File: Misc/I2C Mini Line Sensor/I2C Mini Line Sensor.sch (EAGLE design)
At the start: 16 parts, among them U1 ADS1015.RUG, U2 QRE1113, U3 QRE1113, U4 QRE1113, U5 QRE1113

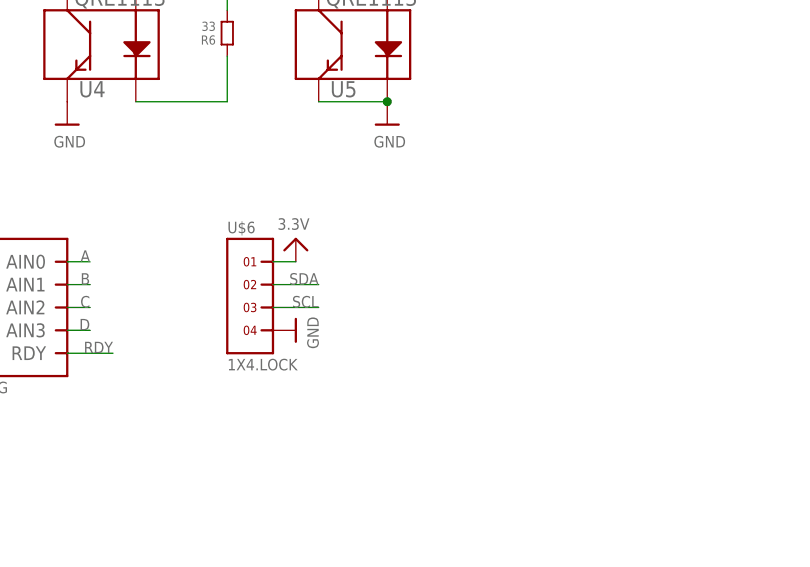
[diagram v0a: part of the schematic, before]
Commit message: Added address select pins for IC
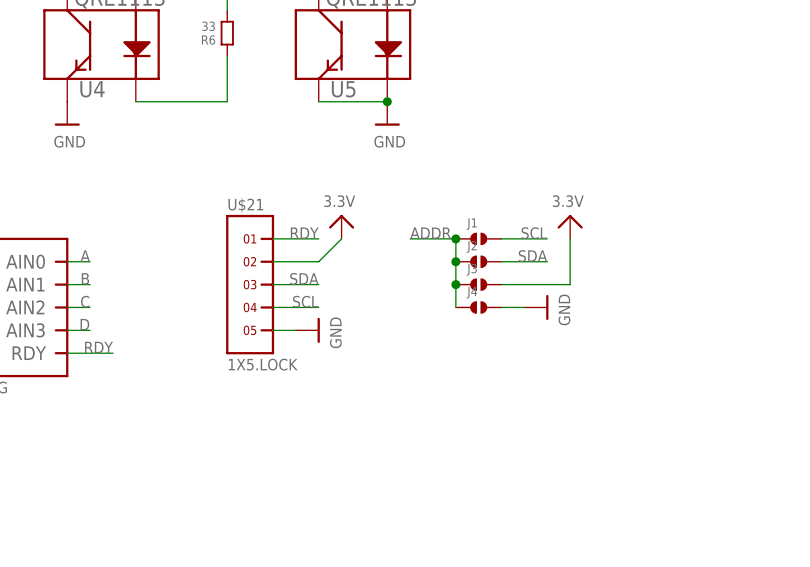
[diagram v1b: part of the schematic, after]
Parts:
- removed U$6: 1X4.LOCK, headers(.1in):1X4.LOCK
- added J1, J2, J3, J4: (no value), solderjumper:SOLDERJUMPER.2.MED
- added U$21: 1X5.LOCK, headers(.1in):1X5.LOCK
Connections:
- net 3.3V: now also J3.2, U$21.2; no longer U$6.1
- net ADDR: now also J1.1, J2.1, J3.1, J4.1
- net GND: now also J4.2, U$21.5; no longer U$6.4
- net RDY: now also U$21.1
- net SCL: now also J1.2, U$21.4; no longer U$6.3
- net SDA: now also J2.2, U$21.3; no longer U$6.2
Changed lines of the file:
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@@
 <part name="U$4" library="microbuilder" deviceset="GND" device=""/>
 <part name="U$5" library="microbuilder" deviceset="3.3V" device=""/>
-<part name="U$6" library="headers(.1in)" deviceset="1X4" device=".LOCK" value="1X4.LOCK"/>
 <part name="U$10" library="microbuilder" deviceset="GND" device=""/>
 <part name="U$11" library="microbuilder" deviceset="3.3V" device=""/>
@@
 <part name="U$15" library="microbuilder" deviceset="GND" device=""/>
 <part name="U$16" library="microbuilder" deviceset="GND" device=""/>
+<part name="J1" library="solderjumper" deviceset="SOLDERJUMPER.2" device=".MED"/>
+<part name="J2" library="solderjumper" deviceset="SOLDERJUMPER.2" device=".MED"/>
+<part name="J3" library="solderjumper" deviceset="SOLDERJUMPER.2" device=".MED"/>
+<part name="J4" library="solderjumper" deviceset="SOLDERJUMPER.2" device=".MED"/>
+<part name="U$17" library="microbuilder" deviceset="3.3V" device=""/>
+<part name="U$20" library="microbuilder" deviceset="GND" device=""/>
+<part name="U$21" library="headers(.1in)" deviceset="1X5" device=".LOCK"/>
 </parts>
 <sheets>
@@
 <instance part="U$4" gate="G$1" x="25.4" y="91.44"/>
 <instance part="U$5" gate="G$1" x="25.4" y="99.06"/>
-<instance part="U$6" gate="G$1" x="86.36" y="96.52"/>
-<instance part="U$10" gate="G$1" x="91.44" y="93.98" rot="MR270"/>
-<instance part="U$11" gate="G$1" x="91.44" y="101.6" rot="MR0"/>
+<instance part="U$10" gate="G$1" x="93.98" y="93.98" rot="MR270"/>
+<instance part="U$11" gate="G$1" x="96.52" y="104.14" rot="MR0"/>
 <instance part="U1" gate="G$1" x="55.88" y="96.52"/>
 <instance part="U$1" gate="G$1" x="45.72" y="104.14"/>
@@
 <instance part="U$15" gate="G$1" x="17.78" y="116.84"/>
 <instance part="U$16" gate="G$1" x="66.04" y="116.84"/>
+<instance part="J1" gate="G$1" x="111.76" y="104.14"/>
+<instance part="J2" gate="G$1" x="111.76" y="101.6"/>
+<instance part="J3" gate="G$1" x="111.76" y="99.06"/>
+<instance part="J4" gate="G$1" x="111.76" y="96.52"/>
+<instance part="U$17" gate="G$1" x="121.92" y="104.14" rot="MR0"/>
+<instance part="U$20" gate="G$1" x="119.38" y="96.52" rot="MR270"/>
+<instance part="U$21" gate="G$1" x="86.36" y="99.06"/>
 </instances>
 <busses>
@@
 </segment>
 <segment>
-<pinref part="U$6" gate="G$1" pin="4"/>
-<pinref part="U$10" gate="G$1" pin="GND"/>
-</segment>
-<segment>
 <pinref part="U1" gate="G$1" pin="GND"/>
 <pinref part="U$14" gate="G$1" pin="GND"/>
@@
 <pinref part="U$16" gate="G$1" pin="GND"/>
 </segment>
+<segment>
+<pinref part="U$20" gate="G$1" pin="GND"/>
+<pinref part="J4" gate="G$1" pin="2"/>
+<wire x1="116.84" y1="96.52" x2="114.3" y2="96.52" width="0.1524" layer="91"/>
+</segment>
+<segment>
+<pinref part="U$10" gate="G$1" pin="GND"/>
+<pinref part="U$21" gate="G$1" pin="5"/>
+<wire x1="91.44" y1="93.98" x2="88.9" y2="93.98" width="0.1524" layer="91"/>
+</segment>
 </net>
 <net name="SDA" class="0">
 <segment>
-<pinref part="U$6" gate="G$1" pin="2"/>
 <wire x1="88.9" y1="99.06" x2="93.98" y2="99.06" width="0.1524" layer="91"/>
 <label x="93.98" y="99.06" size="1.27" layer="95" rot="MR0"/>
+<pinref part="U$21" gate="G$1" pin="3"/>
 </segment>
 <segment>
@@
 <label x="43.18" y="99.06" size="1.27" layer="95"/>
 </segment>
+<segment>
+<pinref part="J2" gate="G$1" pin="2"/>
+<wire x1="119.38" y1="101.6" x2="114.3" y2="101.6" width="0.1524" layer="91"/>
+<label x="119.38" y="101.6" size="1.27" layer="95" rot="MR0"/>
+</segment>
 </net>
 <net name="SCL" class="0">
 <segment>
-<pinref part="U$6" gate="G$1" pin="3"/>
 <wire x1="93.98" y1="96.52" x2="88.9" y2="96.52" width="0.1524" layer="91"/>
 <label x="93.98" y="96.52" size="1.27" layer="95" rot="MR0"/>
+<pinref part="U$21" gate="G$1" pin="4"/>
 </segment>
 <segment>
@@
 <wire x1="43.18" y1="96.52" x2="48.26" y2="96.52" width="0.1524" layer="91"/>
 <label x="43.18" y="96.52" size="1.27" layer="95"/>
+</segment>
+<segment>
+<pinref part="J1" gate="G$1" pin="2"/>
+<wire x1="114.3" y1="104.14" x2="119.38" y2="104.14" width="0.1524" layer="91"/>
+<label x="119.38" y="104.14" size="1.27" layer="95" rot="MR0"/>
 </segment>
 </net>
@@
 </segment>
 <segment>
-<pinref part="U$6" gate="G$1" pin="1"/>
 <pinref part="U$11" gate="G$1" pin="3.3V"/>
-<wire x1="88.9" y1="101.6" x2="91.44" y2="101.6" width="0.1524" layer="91"/>
+<wire x1="88.9" y1="101.6" x2="93.98" y2="101.6" width="0.1524" layer="91"/>
+<wire x1="93.98" y1="101.6" x2="96.52" y2="104.14" width="0.1524" layer="91"/>
+<pinref part="U$21" gate="G$1" pin="2"/>
 </segment>
 <segment>
@@
 <pinref part="U$13" gate="G$1" pin="3.3V"/>
 </segment>
+<segment>
+<pinref part="J3" gate="G$1" pin="2"/>
+<pinref part="U$17" gate="G$1" pin="3.3V"/>
+<wire x1="114.3" y1="99.06" x2="121.92" y2="99.06" width="0.1524" layer="91"/>
+<wire x1="121.92" y1="99.06" x2="121.92" y2="104.14" width="0.1524" layer="91"/>
+</segment>
 </net>
 <net name="ADDR" class="0">
@@
 <label x="43.18" y="93.98" size="1.27" layer="95"/>
 </segment>
+<segment>
+<pinref part="J1" gate="G$1" pin="1"/>
+<pinref part="J2" gate="G$1" pin="1"/>
+<wire x1="109.22" y1="104.14" x2="109.22" y2="101.6" width="0.1524" layer="91"/>
+<pinref part="J3" gate="G$1" pin="1"/>
+<wire x1="109.22" y1="101.6" x2="109.22" y2="99.06" width="0.1524" layer="91"/>
+<junction x="109.22" y="101.6"/>
+<pinref part="J4" gate="G$1" pin="1"/>
+<wire x1="109.22" y1="99.06" x2="109.22" y2="96.52" width="0.1524" layer="91"/>
+<junction x="109.22" y="99.06"/>
+<wire x1="109.22" y1="104.14" x2="104.14" y2="104.14" width="0.1524" layer="91"/>
+<junction x="109.22" y="104.14"/>
+<label x="104.14" y="104.14" size="1.27" layer="95"/>
+</segment>
 </net>
 <net name="RDY" class="0">
@@
 <label x="71.12" y="91.44" size="1.27" layer="95" rot="MR0"/>
 </segment>
-</net>
+<segment>
+<pinref part="U$21" gate="G$1" pin="1"/>
+<wire x1="88.9" y1="104.14" x2="93.98" y2="104.14" width="0.1524" layer="91"/>
+<label x="93.98" y="104.14" size="1.27" layer="95" rot="MR0"/>
+</segment>
+</net>

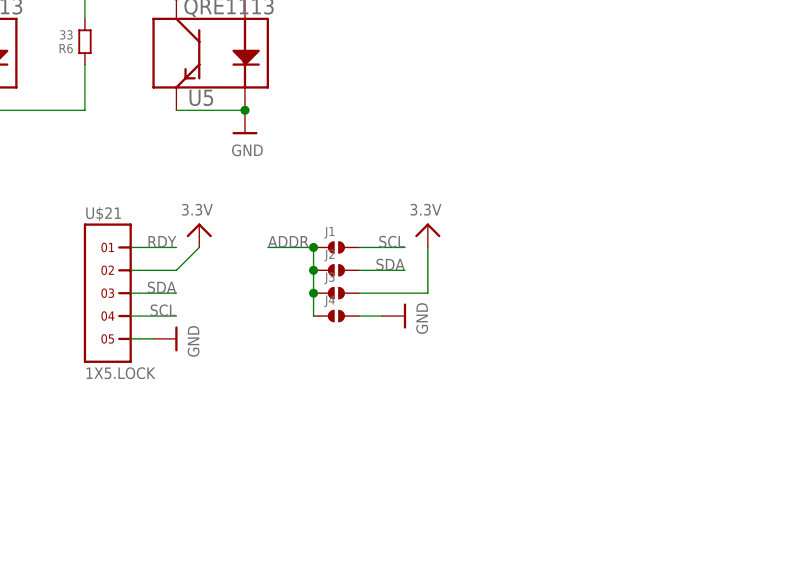
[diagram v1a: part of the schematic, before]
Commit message: Cleaned up layout of I2C Mini Line Sensor and I2C Line Sensor Also geenerated preview images
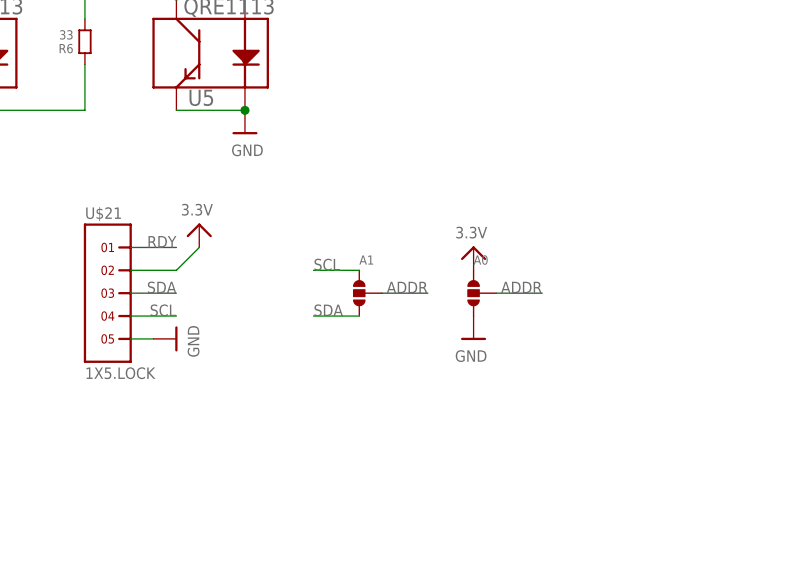
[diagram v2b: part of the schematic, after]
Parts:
- removed J1, J2, J3, J4: (no value), solderjumper:SOLDERJUMPER.2.MED
- added A0, A1: (no value), solderjumper:SOLDERJUMPER.3.MED
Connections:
- net 3.3V: now also A0.1; no longer J3.2
- net ADDR: now also A0.2, A1.2; no longer J1.1, J2.1, J3.1, J4.1
- net GND: now also A0.3; no longer J4.2
- net SCL: now also A1.1; no longer J1.2
- net SDA: now also A1.3; no longer J2.2
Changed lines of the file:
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@@
 <part name="U$15" library="microbuilder" deviceset="GND" device=""/>
 <part name="U$16" library="microbuilder" deviceset="GND" device=""/>
-<part name="J1" library="solderjumper" deviceset="SOLDERJUMPER.2" device=".MED"/>
-<part name="J2" library="solderjumper" deviceset="SOLDERJUMPER.2" device=".MED"/>
-<part name="J3" library="solderjumper" deviceset="SOLDERJUMPER.2" device=".MED"/>
-<part name="J4" library="solderjumper" deviceset="SOLDERJUMPER.2" device=".MED"/>
 <part name="U$17" library="microbuilder" deviceset="3.3V" device=""/>
 <part name="U$20" library="microbuilder" deviceset="GND" device=""/>
 <part name="U$21" library="headers(.1in)" deviceset="1X5" device=".LOCK"/>
+<part name="A1" library="solderjumper" deviceset="SOLDERJUMPER.3" device=".MED"/>
+<part name="A0" library="solderjumper" deviceset="SOLDERJUMPER.3" device=".MED"/>
 </parts>
 <sheets>
@@
 <instance part="U$15" gate="G$1" x="17.78" y="116.84"/>
 <instance part="U$16" gate="G$1" x="66.04" y="116.84"/>
-<instance part="J1" gate="G$1" x="111.76" y="104.14"/>
-<instance part="J2" gate="G$1" x="111.76" y="101.6"/>
-<instance part="J3" gate="G$1" x="111.76" y="99.06"/>
-<instance part="J4" gate="G$1" x="111.76" y="96.52"/>
-<instance part="U$17" gate="G$1" x="121.92" y="104.14" rot="MR0"/>
-<instance part="U$20" gate="G$1" x="119.38" y="96.52" rot="MR270"/>
+<instance part="U$17" gate="G$1" x="127" y="101.6" rot="MR0"/>
+<instance part="U$20" gate="G$1" x="127" y="93.98" rot="MR0"/>
 <instance part="U$21" gate="G$1" x="86.36" y="99.06"/>
+<instance part="A1" gate="G$1" x="114.3" y="99.06"/>
+<instance part="A0" gate="G$1" x="127" y="99.06"/>
 </instances>
 <busses>
@@
 </segment>
 <segment>
-<pinref part="U$20" gate="G$1" pin="GND"/>
-<pinref part="J4" gate="G$1" pin="2"/>
-<wire x1="116.84" y1="96.52" x2="114.3" y2="96.52" width="0.1524" layer="91"/>
-</segment>
-<segment>
 <pinref part="U$10" gate="G$1" pin="GND"/>
 <pinref part="U$21" gate="G$1" pin="5"/>
 <wire x1="91.44" y1="93.98" x2="88.9" y2="93.98" width="0.1524" layer="91"/>
 </segment>
+<segment>
+<pinref part="A0" gate="G$1" pin="3"/>
+<pinref part="U$20" gate="G$1" pin="GND"/>
+</segment>
 </net>
 <net name="SDA" class="0">
@@
 </segment>
 <segment>
-<pinref part="J2" gate="G$1" pin="2"/>
-<wire x1="119.38" y1="101.6" x2="114.3" y2="101.6" width="0.1524" layer="91"/>
-<label x="119.38" y="101.6" size="1.27" layer="95" rot="MR0"/>
+<pinref part="A1" gate="G$1" pin="3"/>
+<wire x1="109.22" y1="96.52" x2="114.3" y2="96.52" width="0.1524" layer="91"/>
+<label x="109.22" y="96.52" size="1.27" layer="95"/>
 </segment>
 </net>
@@
 </segment>
 <segment>
-<pinref part="J1" gate="G$1" pin="2"/>
-<wire x1="114.3" y1="104.14" x2="119.38" y2="104.14" width="0.1524" layer="91"/>
-<label x="119.38" y="104.14" size="1.27" layer="95" rot="MR0"/>
+<pinref part="A1" gate="G$1" pin="1"/>
+<wire x1="114.3" y1="101.6" x2="109.22" y2="101.6" width="0.1524" layer="91"/>
+<label x="109.22" y="101.6" size="1.27" layer="95"/>
 </segment>
 </net>
@@
 </segment>
 <segment>
-<pinref part="J3" gate="G$1" pin="2"/>
+<pinref part="A0" gate="G$1" pin="1"/>
 <pinref part="U$17" gate="G$1" pin="3.3V"/>
-<wire x1="114.3" y1="99.06" x2="121.92" y2="99.06" width="0.1524" layer="91"/>
-<wire x1="121.92" y1="99.06" x2="121.92" y2="104.14" width="0.1524" layer="91"/>
 </segment>
 </net>
@@
 </segment>
 <segment>
-<pinref part="J1" gate="G$1" pin="1"/>
-<pinref part="J2" gate="G$1" pin="1"/>
-<wire x1="109.22" y1="104.14" x2="109.22" y2="101.6" width="0.1524" layer="91"/>
-<pinref part="J3" gate="G$1" pin="1"/>
-<wire x1="109.22" y1="101.6" x2="109.22" y2="99.06" width="0.1524" layer="91"/>
-<junction x="109.22" y="101.6"/>
-<pinref part="J4" gate="G$1" pin="1"/>
-<wire x1="109.22" y1="99.06" x2="109.22" y2="96.52" width="0.1524" layer="91"/>
-<junction x="109.22" y="99.06"/>
-<wire x1="109.22" y1="104.14" x2="104.14" y2="104.14" width="0.1524" layer="91"/>
-<junction x="109.22" y="104.14"/>
-<label x="104.14" y="104.14" size="1.27" layer="95"/>
-</segment>
-</net>
+<wire x1="129.54" y1="99.06" x2="134.62" y2="99.06" width="0.1524" layer="91"/>
+<label x="134.62" y="99.06" size="1.27" layer="95" rot="MR0"/>
+<pinref part="A0" gate="G$1" pin="2"/>
+</segment>
+<segment>
+<pinref part="A1" gate="G$1" pin="2"/>
+<wire x1="116.84" y1="99.06" x2="121.92" y2="99.06" width="0.1524" layer="91"/>
+<label x="121.92" y="99.06" size="1.27" layer="95" rot="MR0"/>
+</segment>
+</net>

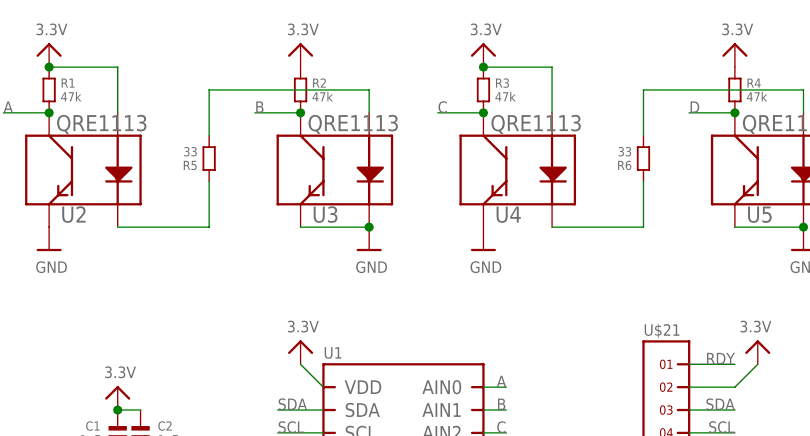
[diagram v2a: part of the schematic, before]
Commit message: Modified resistor values such that the PCBs should no longer get hot
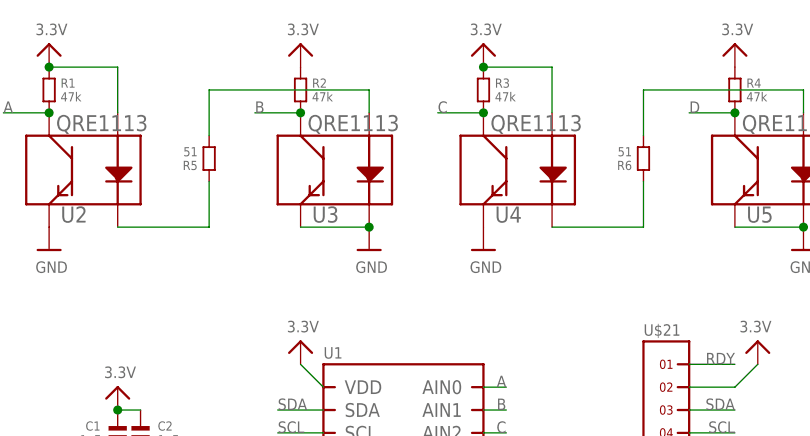
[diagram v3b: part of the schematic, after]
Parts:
- R5, R6: value 33 -> 51
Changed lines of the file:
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@@
 <grid distance="0.1" unitdist="inch" unit="inch" style="lines" multiple="1" display="no" altdistance="0.01" altunitdist="inch" altunit="inch"/>
 <layers>
-<layer number="1" name="Top" color="4" fill="1" visible="yes" active="no"/>
-<layer number="16" name="Bottom" color="1" fill="1" visible="yes" active="no"/>
-<layer number="17" name="Pads" color="2" fill="1" visible="yes" active="no"/>
-<layer number="18" name="Vias" color="2" fill="1" visible="yes" active="no"/>
-<layer number="19" name="Unrouted" color="6" fill="1" visible="yes" active="no"/>
-<layer number="20" name="Dimension" color="15" fill="1" visible="yes" active="no"/>
-<layer number="21" name="tPlace" color="7" fill="1" visible="yes" active="no"/>
-<layer number="22" name="bPlace" color="7" fill="1" visible="yes" active="no"/>
-<layer number="23" name="tOrigins" color="15" fill="1" visible="yes" active="no"/>
-<layer number="24" name="bOrigins" color="15" fill="1" visible="yes" active="no"/>
-<layer number="25" name="tNames" color="7" fill="1" visible="yes" active="no"/>
-<layer number="26" name="bNames" color="7" fill="1" visible="yes" active="no"/>
-<layer number="27" name="tValues" color="7" fill="1" visible="yes" active="no"/>
-<layer number="28" name="bValues" color="7" fill="1" visible="yes" active="no"/>
+<layer number="1" name="Top" color="4" fill="1" visible="no" active="no"/>
+<layer number="16" name="Bottom" color="1" fill="1" visible="no" active="no"/>
+<layer number="17" name="Pads" color="2" fill="1" visible="no" active="no"/>
+<layer number="18" name="Vias" color="2" fill="1" visible="no" active="no"/>
+<layer number="19" name="Unrouted" color="6" fill="1" visible="no" active="no"/>
+<layer number="20" name="Dimension" color="15" fill="1" visible="no" active="no"/>
+<layer number="21" name="tPlace" color="7" fill="1" visible="no" active="no"/>
+<layer number="22" name="bPlace" color="7" fill="1" visible="no" active="no"/>
+<layer number="23" name="tOrigins" color="15" fill="1" visible="no" active="no"/>
+<layer number="24" name="bOrigins" color="15" fill="1" visible="no" active="no"/>
+<layer number="25" name="tNames" color="7" fill="1" visible="no" active="no"/>
+<layer number="26" name="bNames" color="7" fill="1" visible="no" active="no"/>
+<layer number="27" name="tValues" color="7" fill="1" visible="no" active="no"/>
+<layer number="28" name="bValues" color="7" fill="1" visible="no" active="no"/>
 <layer number="29" name="tStop" color="7" fill="3" visible="no" active="no"/>
 <layer number="30" name="bStop" color="7" fill="6" visible="no" active="no"/>
@@
 <layer number="35" name="tGlue" color="7" fill="4" visible="no" active="no"/>
 <layer number="36" name="bGlue" color="7" fill="5" visible="no" active="no"/>
-<layer number="37" name="tTest" color="7" fill="1" visible="yes" active="no"/>
-<layer number="38" name="bTest" color="7" fill="1" visible="yes" active="no"/>
+<layer number="37" name="tTest" color="7" fill="1" visible="no" active="no"/>
+<layer number="38" name="bTest" color="7" fill="1" visible="no" active="no"/>
 <layer number="39" name="tKeepout" color="4" fill="11" visible="no" active="no"/>
 <layer number="40" name="bKeepout" color="1" fill="11" visible="no" active="no"/>
@@
 <layer number="44" name="Drills" color="7" fill="1" visible="no" active="no"/>
 <layer number="45" name="Holes" color="7" fill="1" visible="no" active="no"/>
-<layer number="46" name="Milling" color="3" fill="1" visible="yes" active="no"/>
-<layer number="47" name="Measures" color="7" fill="1" visible="yes" active="no"/>
-<layer number="48" name="Document" color="7" fill="1" visible="yes" active="no"/>
-<layer number="49" name="Reference" color="7" fill="1" visible="yes" active="no"/>
-<layer number="50" name="dxf" color="7" fill="1" visible="yes" active="no"/>
-<layer number="51" name="tDocu" color="7" fill="1" visible="yes" active="no"/>
-<layer number="52" name="bDocu" color="7" fill="1" visible="yes" active="no"/>
-<layer number="53" name="tGND_GNDA" color="7" fill="9" visible="yes" active="no"/>
-<layer number="54" name="bGND_GNDA" color="1" fill="9" visible="yes" active="no"/>
-<layer number="56" name="wert" color="7" fill="1" visible="yes" active="no"/>
+<layer number="46" name="Milling" color="3" fill="1" visible="no" active="no"/>
+<layer number="47" name="Measures" color="7" fill="1" visible="no" active="no"/>
+<layer number="48" name="Document" color="7" fill="1" visible="no" active="no"/>
+<layer number="49" name="Reference" color="7" fill="1" visible="no" active="no"/>
+<layer number="50" name="dxf" color="7" fill="1" visible="no" active="no"/>
+<layer number="51" name="tDocu" color="7" fill="1" visible="no" active="no"/>
+<layer number="52" name="bDocu" color="7" fill="1" visible="no" active="no"/>
+<layer number="53" name="tGND_GNDA" color="7" fill="9" visible="no" active="no"/>
+<layer number="54" name="bGND_GNDA" color="1" fill="9" visible="no" active="no"/>
+<layer number="56" name="wert" color="7" fill="1" visible="no" active="no"/>
 <layer number="91" name="Nets" color="2" fill="1" visible="yes" active="yes"/>
 <layer number="92" name="Busses" color="1" fill="1" visible="yes" active="yes"/>
@@
 <part name="R3" library="standardparts" deviceset="RESISTOR" device=".0603" value="47k"/>
 <part name="R4" library="standardparts" deviceset="RESISTOR" device=".0603" value="47k"/>
-<part name="R5" library="standardparts" deviceset="RESISTOR" device=".0603" value="33"/>
-<part name="R6" library="standardparts" deviceset="RESISTOR" device=".0603" value="33"/>
+<part name="R5" library="standardparts" deviceset="RESISTOR" device=".0603" value="51"/>
+<part name="R6" library="standardparts" deviceset="RESISTOR" device=".0603" value="51"/>
 <part name="U$2" library="microbuilder" deviceset="3.3V" device=""/>
 <part name="U$7" library="microbuilder" deviceset="GND" device=""/>
